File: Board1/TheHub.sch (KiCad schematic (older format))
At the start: 55 parts, among them J1 ARM_ADC_1, J10 SCIENCE + WHEELS POWER CONN, J11 RFD900, J12 I2C_1 Test Point, J13 I2C_2 Test Point, J14 ARDUINO NANO LEFT, J15 GPIO Test, J16 I2C_3 Test Point, J17 12V OUT, J18 7.4V IN, J19 ANALOG SENSORS, J2 ARM_ADC_2, J20 GPS, J21 COMPASS, J22 ARDUINO NANO RIGHT, J23 NucleoRight, J3 ARM_PWM_OUT, J4 ARM POWER CONN, J5 NucleoLeft, J6 SCI_ADC_1, J7 SCIENCE_PWM_OUT, J8 12V MAIN POWER, J9 WHEEL_ADC_1, U1 PRE-PCA9685, U2 PRE-ADS1115, U3 PRE-ADS1115, U4 PRE-PCA9685, U5 PRE-ADS1115, U6 TL1963, U7 LM340MP-5.0, U9 PRE-ADS1115

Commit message: Add note or BNO055, add GPS, add nucleo pin declaration for GPS_FIX GPIO_Input
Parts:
- added U?: ADXL377, symbol ADXL377
- added U?: BNO055, symbol BNO055
- added U?: MCP9808, symbol MCP9808
- added U?: MPL115A2, symbol MPL115A2
- added U?: GPS, symbol GPS
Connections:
- net labels added: GPS_FIX, PWM1, PWM2
- wire segments 150 -> 161
- no-connect marks 52 -> 70
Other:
- note added: "GPS_FIX is HIGH when\nthe unit has a GPS lock."
- note added: "PS0 and PS1 are protocol select pins. \nLeave them connected to ground through\n 10k resistors for standard/fast I2C.\n"
- moved on the sheet: D7, R13

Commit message: Annotate schematic
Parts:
- gave numbers to parts that had none: 5

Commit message: Add MPL115A2 footprint, annotate schematic
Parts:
- removed D7: LED, LEDs:LED_0805, symbol LED
- removed J1: ARM_ADC_1, Pin_Headers:Pin_Header_Straight_2x04_Pitch2.54mm, symbol CONN_02X04
- removed J10: SCIENCE + WHEELS POWER CONN, Pin_Headers:Pin_Header_Straight_2x19_Pitch2.54mm, symbol CONN_02X16
- removed J14: ARDUINO NANO LEFT, Socket_Strips:Socket_Strip_Straight_1x15_Pitch2.54mm, symbol CONN_01X15
- removed J19: ANALOG SENSORS, Pin_Headers:Pin_Header_Straight_2x05_Pitch2.54mm, symbol CONN_02X05
- removed J2: ARM_ADC_2, Pin_Headers:Pin_Header_Straight_2x04_Pitch2.54mm, symbol CONN_02X04
- removed J20: GPS, Socket_Strips:Socket_Strip_Straight_1x09_Pitch2.54mm, symbol CONN_01X09
- removed J21: COMPASS, Socket_Strips:Socket_Strip_Straight_1x06_Pitch2.54mm, symbol CONN_01X06
- removed J22: ARDUINO NANO RIGHT, Socket_Strips:Socket_Strip_Straight_1x15_Pitch2.54mm, symbol CONN_01X15
- removed J3: ARM_PWM_OUT, Pin_Headers:Pin_Header_Straight_1x16_Pitch2.54mm, symbol CONN_01X16
- removed J4: ARM POWER CONN, Pin_Headers:Pin_Header_Straight_2x16_Pitch2.54mm, symbol CONN_02X16
- removed J6: SCI_ADC_1, Pin_Headers:Pin_Header_Straight_2x04_Pitch2.54mm, symbol CONN_02X04
- removed J7: SCIENCE_PWM_OUT, Pin_Headers:Pin_Header_Straight_1x16_Pitch2.54mm, symbol CONN_01X16
- removed J9: WHEEL_ADC_1, Pin_Headers:Pin_Header_Straight_2x04_Pitch2.54mm, symbol CONN_02X04
- removed R13: 220, Resistors_SMD:R_0805, symbol R
- removed U1, U4: PRE-PCA9685, FoxWestern:PCA9685, symbol PRE-PCA9685
- removed U2, U3, U5, U9: PRE-ADS1115, Socket_Strips:Socket_Strip_Straight_1x10_Pitch2.54mm, symbol PRE-ADS1115
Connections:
- net labels removed: A3, A4, A5, A6, A7, D10, D11, D12, D13, D2, D3, D4, D5, D6, D7, D8, D9, REF, RX0, TX1, VIN
- wire segments 161 -> 88
- no-connect marks 70 -> 37
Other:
- note added: "1.0"
- note added: "1/8/2017"
- note added: "2.2k pullups allow for fast I2C. Test headers allow for easy testing."
- note added: "Lin reg for powering microcontroller + sensors"
- note added: "Lin regs used to save money and reduce noise and complexity"
- note added: "Made By: Danny Mallek"
- note added: "Test Board"
- note added: "lin reg for rfd900"
- note removed: "0X48\n"
- note removed: "0X49"
- note removed: "0X4A"
- note removed: "0X4B"
- note removed: "ARM CARD"
- note removed: "AUTONOMY CARD"
- note removed: "SCIENCE +WHEEL CARD"
- note removed: "SOLDER 00000: 0X40"
- note removed: "SOLDER 00001: 0X41"
- note removed: "USE ADAFRUIT HMC5883L\nFOR COMPATIBILITY"
- note removed: "USE ADAFRUIT ULTIMATE GPS\nFOR COMPATIBILITY"

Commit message: Associate parts using CvPCB
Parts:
- U10: footprint (none) -> FoxWestern:ADXL377
- U11: footprint (none) -> FoxWestern:BNO055
- U12: footprint (none) -> FoxWestern:MPL115A2
- U13: footprint (none) -> FoxWestern:Adafruit_GPS
- U8: footprint (none) -> FoxWestern:MCP9808
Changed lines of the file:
@@
 5V
 $Comp
-L +5V #PWR028
+L +5V #PWR014
 U 1 1 593718A3
 P 12650 1550
-F 0 "#PWR028" H 12650 1400 50  0001 C CNN
+F 0 "#PWR014" H 12650 1400 50  0001 C CNN
 F 1 "+5V" H 12650 1690 50  0000 C CNN
 F 2 "" H 12650 1550 50  0001 C CNN
@@
 $EndComp
 $Comp
-L GND #PWR029
+L GND #PWR015
 U 1 1 59371A35
 P 12150 1250
-F 0 "#PWR029" H 12150 1000 50  0001 C CNN
+F 0 "#PWR015" H 12150 1000 50  0001 C CNN
 F 1 "GND" H 12150 1100 50  0000 C CNN
 F 2 "" H 12150 1250 50  0001 C CNN
@@
 USART6_RX
 $Comp
-L GND #PWR030
+L GND #PWR016
 U 1 1 59372AF7
 P 12550 2150
-F 0 "#PWR030" H 12550 1900 50  0001 C CNN
+F 0 "#PWR016" H 12550 1900 50  0001 C CNN
 F 1 "GND" H 12550 2000 50  0000 C CNN
 F 2 "" H 12550 2150 50  0001 C CNN
@@
 $EndComp
 $Comp
-L GND #PWR031
+L GND #PWR017
 U 1 1 59376B06
 P 13250 2200
-F 0 "#PWR031" H 13250 1950 50  0001 C CNN
+F 0 "#PWR017" H 13250 1950 50  0001 C CNN
 F 1 "GND" H 13250 2050 50  0000 C CNN
 F 2 "" H 13250 2200 50  0001 C CNN
@@
 $EndComp
 $Comp
-L GND #PWR032
+L GND #PWR018
 U 1 1 593775C1
 P 14050 2200
-F 0 "#PWR032" H 14050 1950 50  0001 C CNN
+F 0 "#PWR018" H 14050 1950 50  0001 C CNN
 F 1 "GND" H 14050 2050 50  0000 C CNN
 F 2 "" H 14050 2200 50  0001 C CNN
@@
 $EndComp
 $Comp
-L GND #PWR033
+L GND #PWR019
 U 1 1 5937761C
 P 15050 2200
-F 0 "#PWR033" H 15050 1950 50  0001 C CNN
+F 0 "#PWR019" H 15050 1950 50  0001 C CNN
 F 1 "GND" H 15050 2050 50  0000 C CNN
 F 2 "" H 15050 2200 50  0001 C CNN
@@
 $EndComp
 $Comp
-L GND #PWR034
+L GND #PWR020
 U 1 1 5937D087
 P 13650 3350
-F 0 "#PWR034" H 13650 3100 50  0001 C CNN
+F 0 "#PWR020" H 13650 3100 50  0001 C CNN
 F 1 "GND" H 13650 3200 50  0000 C CNN
 F 2 "" H 13650 3350 50  0001 C CNN
@@
 $EndComp
 $Comp
-L +12V #PWR035
+L +12V #PWR021
 U 1 1 5937F443
 P 9250 3100
-F 0 "#PWR035" H 9250 2950 50  0001 C CNN
+F 0 "#PWR021" H 9250 2950 50  0001 C CNN
 F 1 "+12V" H 9250 3240 50  0000 C CNN
 F 2 "" H 9250 3100 50  0001 C CNN
@@
 $EndComp
 $Comp
-L +5V #PWR036
+L +5V #PWR022
 U 1 1 59380CDB
 P 10600 3050
-F 0 "#PWR036" H 10600 2900 50  0001 C CNN
+F 0 "#PWR022" H 10600 2900 50  0001 C CNN
 F 1 "+5V" H 10600 3190 50  0000 C CNN
 F 2 "" H 10600 3050 50  0001 C CNN
@@
 $EndComp
 $Comp
-L GND #PWR037
+L GND #PWR023
 U 1 1 59381160
 P 9900 3700
-F 0 "#PWR037" H 9900 3450 50  0001 C CNN
+F 0 "#PWR023" H 9900 3450 50  0001 C CNN
 F 1 "GND" H 9900 3550 50  0000 C CNN
 F 2 "" H 9900 3700 50  0001 C CNN
@@
 $EndComp
 $Comp
-L PWR_FLAG #FLG038
+L PWR_FLAG #FLG024
 U 1 1 59381518
 P 10600 1500
-F 0 "#FLG038" H 10600 1575 50  0001 C CNN
+F 0 "#FLG024" H 10600 1575 50  0001 C CNN
 F 1 "PWR_FLAG" H 10600 1650 50  0000 C CNN
 F 2 "" H 10600 1500 50  0001 C CNN
@@
 $EndComp
 $Comp
-L PWR_FLAG #FLG039
+L PWR_FLAG #FLG025
 U 1 1 59381757
 P 10600 3200
-F 0 "#FLG039" H 10600 3275 50  0001 C CNN
+F 0 "#FLG025" H 10600 3275 50  0001 C CNN
 F 1 "PWR_FLAG" H 10600 3350 50  0000 C CNN
 F 2 "" H 10600 3200 50  0001 C CNN
@@
 $EndComp
 $Comp
-L GND #PWR040
+L GND #PWR026
 U 1 1 59383C45
 P 11000 2250
-F 0 "#PWR040" H 11000 2000 50  0001 C CNN
+F 0 "#PWR026" H 11000 2000 50  0001 C CNN
 F 1 "GND" H 11000 2100 50  0000 C CNN
 F 2 "" H 11000 2250 50  0001 C CNN
@@
 $EndComp
 $Comp
-L GND #PWR041
+L GND #PWR027
 U 1 1 59383CE4
 P 11100 3700
-F 0 "#PWR041" H 11100 3450 50  0001 C CNN
+F 0 "#PWR027" H 11100 3450 50  0001 C CNN
 F 1 "GND" H 11100 3550 50  0000 C CNN
 F 2 "" H 11100 3700 50  0001 C CNN
@@
 $EndComp
 $Comp
-L +12V #PWR053
+L +12V #PWR028
 U 1 1 593A2E97
 P 7800 2100
-F 0 "#PWR053" H 7800 1950 50  0001 C CNN
+F 0 "#PWR028" H 7800 1950 50  0001 C CNN
 F 1 "+12V" H 7800 2240 50  0000 C CNN
 F 2 "" H 7800 2100 50  0001 C CNN
@@
 $EndComp
 $Comp
-L GND #PWR054
+L GND #PWR029
 U 1 1 593A2EA3
 P 7800 2300
-F 0 "#PWR054" H 7800 2050 50  0001 C CNN
+F 0 "#PWR029" H 7800 2050 50  0001 C CNN
 F 1 "GND" H 7800 2150 50  0000 C CNN
 F 2 "" H 7800 2300 50  0001 C CNN
@@
 $EndComp
 $Comp
-L GND #PWR055
+L GND #PWR030
 U 1 1 593A3BC4
 P 7800 3000
-F 0 "#PWR055" H 7800 2750 50  0001 C CNN
+F 0 "#PWR030" H 7800 2750 50  0001 C CNN
 F 1 "GND" H 7800 2850 50  0000 C CNN
 F 2 "" H 7800 3000 50  0001 C CNN
@@
 	3650 2650 4050 2650
 $Comp
-L +3V3 #PWR060
+L +3V3 #PWR031
 U 1 1 59365D75
 P 4050 2650
-F 0 "#PWR060" H 4050 2500 50  0001 C CNN
+F 0 "#PWR031" H 4050 2500 50  0001 C CNN
 F 1 "+3V3" H 4050 2790 50  0000 C CNN
 F 2 "" H 4050 2650 50  0001 C CNN
@@
 F 0 "U10" H 2950 4600 60  0000 C CNN
 F 1 "ADXL377" H 2800 5400 60  0000 C CNN
-F 2 "" H 2750 5150 60  0001 C CNN
+F 2 "FoxWestern:ADXL377" H 2750 5150 60  0001 C CNN
 F 3 "" H 2750 5150 60  0001 C CNN
 	1    2850 5150
@@
 F 0 "U11" H 5750 5400 60  0000 C CNN
 F 1 "BNO055" H 5550 6100 60  0000 C CNN
-F 2 "" H 5450 5500 60  0001 C CNN
+F 2 "FoxWestern:BNO055" H 5450 5500 60  0001 C CNN
 F 3 "" H 5450 5500 60  0001 C CNN
 	1    5450 5500
@@
 F 0 "U8" H 2950 5750 60  0000 C CNN
 F 1 "MCP9808" H 2800 6650 60  0000 C CNN
-F 2 "" H 2800 6350 60  0001 C CNN
+F 2 "FoxWestern:MCP9808" H 2800 6350 60  0001 C CNN
 F 3 "" H 2800 6350 60  0001 C CNN
 	1    2800 6350
@@
 F 0 "U12" H 5750 6400 60  0000 C CNN
 F 1 "MPL115A2" H 5550 7100 60  0000 C CNN
-F 2 "" H 5600 6600 60  0001 C CNN
+F 2 "FoxWestern:MPL115A2" H 5600 6600 60  0001 C CNN
 F 3 "" H 5600 6600 60  0001 C CNN
 	1    5550 6750
@@
 A2
 $Comp
-L GND #PWR061
+L GND #PWR032
 U 1 1 5A529AE0
 P 2350 5200
-F 0 "#PWR061" H 2350 4950 50  0001 C CNN
+F 0 "#PWR032" H 2350 4950 50  0001 C CNN
 F 1 "GND" H 2350 5050 50  0000 C CNN
 F 2 "" H 2350 5200 50  0001 C CNN
@@
 	2350 5200 2400 5200
 $Comp
-L +3V3 #PWR062
+L +3V3 #PWR033
 U 1 1 5A52A014
 P 2400 5000
-F 0 "#PWR062" H 2400 4850 50  0001 C CNN
+F 0 "#PWR033" H 2400 4850 50  0001 C CNN
 F 1 "+3V3" H 2400 5140 50  0000 C CNN
 F 2 "" H 2400 5000 50  0001 C CNN
@@
 NoConn ~ 2400 6550
 $Comp
-L +3V3 #PWR063
+L +3V3 #PWR034
 U 1 1 5A52B4C8
 P 2400 6150
-F 0 "#PWR063" H 2400 6000 50  0001 C CNN
+F 0 "#PWR034" H 2400 6000 50  0001 C CNN
 F 1 "+3V3" H 2400 6290 50  0000 C CNN
 F 2 "" H 2400 6150 50  0001 C CNN
@@
 $EndComp
 $Comp
-L GND #PWR064
+L GND #PWR035
 U 1 1 5A52B584
 P 2100 6250
-F 0 "#PWR064" H 2100 6000 50  0001 C CNN
+F 0 "#PWR035" H 2100 6000 50  0001 C CNN
 F 1 "GND" H 2100 6100 50  0000 C CNN
 F 2 "" H 2100 6250 50  0001 C CNN
@@
 SCL_1
 $Comp
-L +3V3 #PWR065
+L +3V3 #PWR036
 U 1 1 5A52EB6E
 P 5100 7000
-F 0 "#PWR065" H 5100 6850 50  0001 C CNN
+F 0 "#PWR036" H 5100 6850 50  0001 C CNN
 F 1 "+3V3" H 5100 7140 50  0000 C CNN
 F 2 "" H 5100 7000 50  0001 C CNN
@@
 $EndComp
 $Comp
-L GND #PWR066
+L GND #PWR037
 U 1 1 5A52EBF1
 P 4900 6900
-F 0 "#PWR066" H 4900 6650 50  0001 C CNN
+F 0 "#PWR037" H 4900 6650 50  0001 C CNN
 F 1 "GND" H 4900 6750 50  0000 C CNN
 F 2 "" H 4900 6900 50  0001 C CNN
@@
 NoConn ~ 5100 6500
 $Comp
-L +3V3 #PWR067
+L +3V3 #PWR038
 U 1 1 5A52F8E1
 P 5050 5000
-F 0 "#PWR067" H 5050 4850 50  0001 C CNN
+F 0 "#PWR038" H 5050 4850 50  0001 C CNN
 F 1 "+3V3" H 5050 5140 50  0000 C CNN
 F 2 "" H 5050 5000 50  0001 C CNN
@@
 $EndComp
 $Comp
-L GND #PWR068
+L GND #PWR039
 U 1 1 5A52F99D
 P 4800 5200
-F 0 "#PWR068" H 4800 4950 50  0001 C CNN
+F 0 "#PWR039" H 4800 4950 50  0001 C CNN
 F 1 "GND" H 4800 5050 50  0000 C CNN
 F 2 "" H 4800 5200 50  0001 C CNN
@@
 F 0 "U13" H 8400 6200 60  0000 C CNN
 F 1 "GPS" H 8200 7200 60  0000 C CNN
-F 2 "" H 8150 6950 60  0001 C CNN
+F 2 "FoxWestern:Adafruit_GPS" H 8150 6950 60  0001 C CNN
 F 3 "" H 8150 6950 60  0001 C CNN
 	1    8200 6700
@@
 $EndComp
 $Comp
-L +3V3 #PWR069
+L +3V3 #PWR040
 U 1 1 5A533C10
 P 7750 7000
-F 0 "#PWR069" H 7750 6850 50  0001 C CNN
+F 0 "#PWR040" H 7750 6850 50  0001 C CNN
 F 1 "+3V3" H 7750 7140 50  0000 C CNN
 F 2 "" H 7750 7000 50  0001 C CNN
@@
 $EndComp
 $Comp
-L GND #PWR070
+L GND #PWR041
 U 1 1 5A533CCF
 P 7550 6900
-F 0 "#PWR070" H 7550 6650 50  0001 C CNN
+F 0 "#PWR041" H 7550 6650 50  0001 C CNN
 F 1 "GND" H 7550 6750 50  0000 C CNN
 F 2 "" H 7550 6900 50  0001 C CNN

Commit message: Add to schematic and CubeMX: IO for SD card datalogger, 2x analog pot inputs, quad encoder
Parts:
- added J?: Actuator Fdbk Conn, symbol Conn_02x03_Odd_Even
- added J?: QuadEnc_Conn, symbol Conn_01x04
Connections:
- net +3V3: now also J?.1 (Pin_1), J?.3 (Pin_3), J?.4 (Pin_4)
- net GND: now also J?.4 (Pin_4), J?.5 (Pin_5), J?.6 (Pin_6)
- net PB13: now also J?.3 (Pin_3)
- net PB14: now also J?.2 (Pin_2)
- net PC0 renamed A_FDBK_1
- net A_FDBK_1: now also J?.2 (Pin_2)
- net PC1 renamed A_FDBK_0
- net A_FDBK_0: now also J?.1 (Pin_1)
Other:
- note added: "With 220Ohm, each led pulls 5mA, for a total of 20mA.\nDo not exceed 200mA for entire chip and 20mA per pin group."
- note removed: "With 220Ohm, each led pulls 5mA, for a total of 20mA."
- moved on the sheet: J5

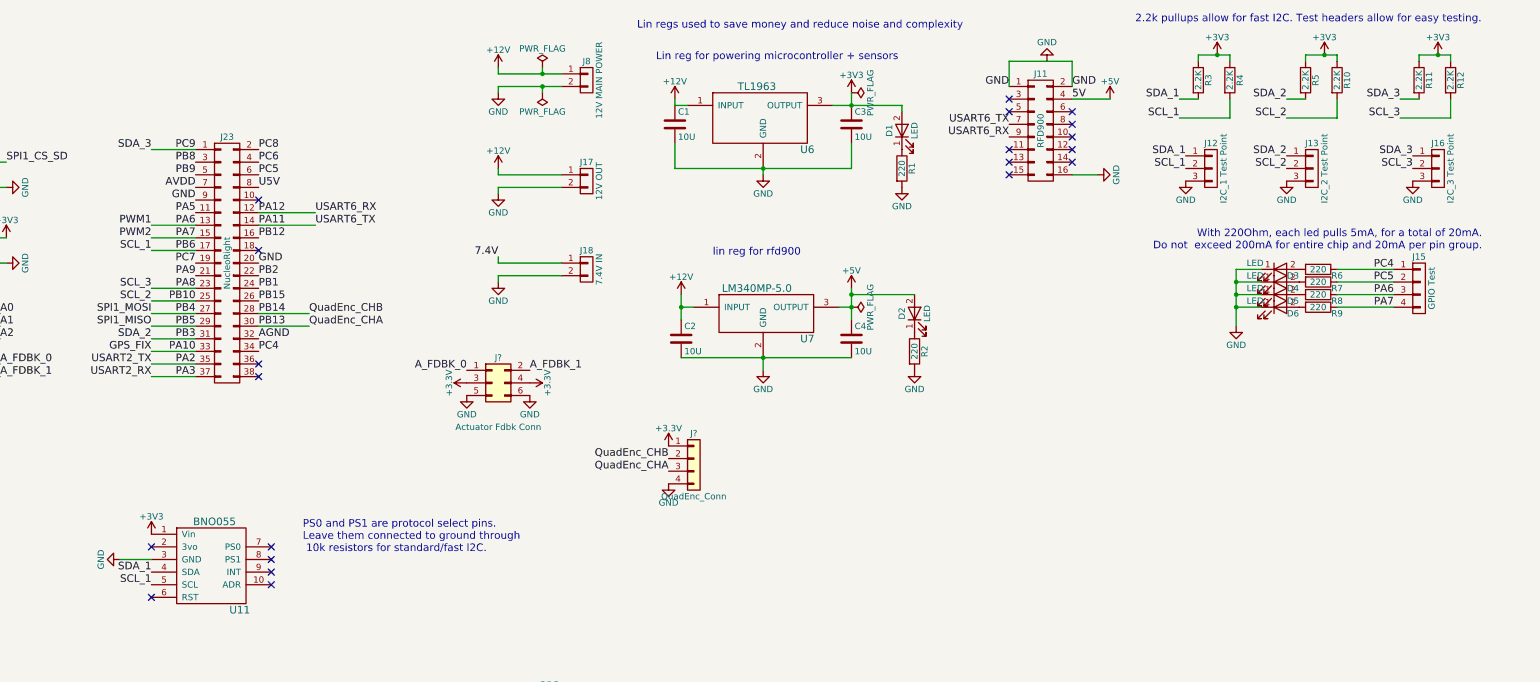
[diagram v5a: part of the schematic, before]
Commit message: Add Datalogger library schematic and integrate into schematic
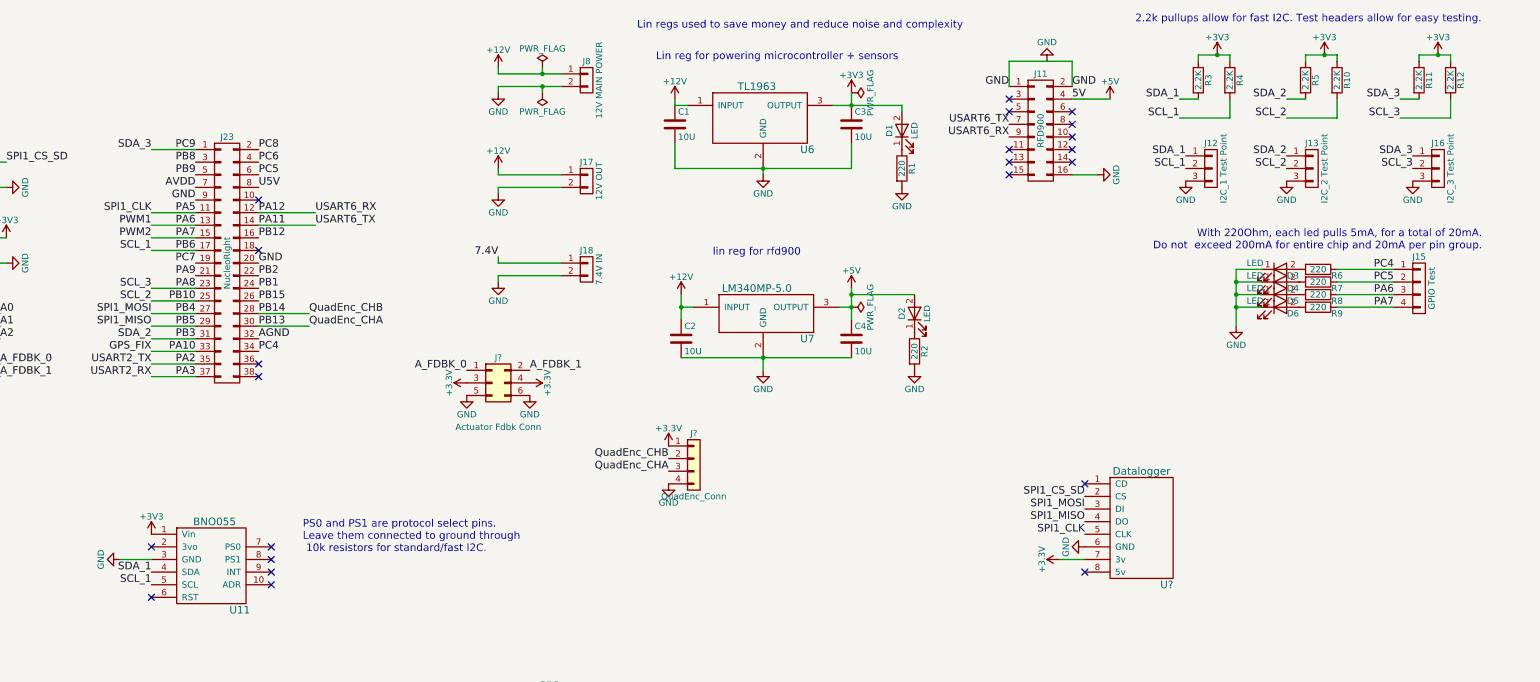
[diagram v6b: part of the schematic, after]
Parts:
- added U?: Datalogger, symbol Datalogger
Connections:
- net +3V3: now also U?.7 (3v)
- net GND: now also U?.6 (GND)
- net PA5: now also U?.5 (CLK)
- net PB4: now also U?.3 (DI)
- net PB5: now also U?.4 (DO)
- net PD2: now also U?.2 (CS)
- no-connect marks 37 -> 39
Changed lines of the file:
@@
 	10600 1500 10600 1600
 Wire Wire Line
-	10450 1600 10600 1600
-Wire Wire Line
-	10600 1600 11000 1600
+	10450 1600 11000 1600
 Wire Wire Line
 	7800 1300 7800 1350
 Wire Wire Line
-	7800 1350 8150 1350
-Wire Wire Line
-	8150 1350 8300 1350
+	7800 1350 8300 1350
 Wire Wire Line
 	8150 1300 8150 1350
@@
 	7800 1500 7800 1450
 Wire Wire Line
-	7800 1450 8150 1450
-Wire Wire Line
-	8150 1450 8300 1450
+	7800 1450 8300 1450
 Wire Wire Line
 	8150 1500 8150 1450
@@
 	15100 1250 15100 1200
 Wire Wire Line
-	15100 1200 15250 1200
-Wire Wire Line
-	15250 1200 15350 1200
+	15100 1200 15350 1200
 Wire Wire Line
 	14950 1700 15350 1700
@@
 	13350 1250 13350 1200
 Wire Wire Line
-	13350 1200 13500 1200
-Wire Wire Line
-	13500 1200 13600 1200
+	13350 1200 13600 1200
 Wire Wire Line
 	13200 1700 13600 1700
@@
 	14200 1250 14200 1200
 Wire Wire Line
-	14200 1200 14350 1200
-Wire Wire Line
-	14350 1200 14450 1200
+	14200 1200 14450 1200
 Wire Wire Line
 	14050 1700 14450 1700
@@
 	9200 1900 9200 2100
 Wire Wire Line
-	9200 2100 9900 2100
-Wire Wire Line
-	9900 2100 10600 2100
+	9200 2100 10600 2100
 Wire Wire Line
 	10600 2100 10600 1900
@@
 	14450 3200 14900 3200
 Wire Wire Line
-	13650 2900 13650 3000
-Wire Wire Line
-	13650 3000 13650 3100
-Wire Wire Line
-	13650 3100 13650 3200
-Wire Wire Line
-	13650 3200 13650 3350
+	13650 2900 13650 3350
 Wire Wire Line
 	13650 2900 13850 2900
@@
 Connection ~ 13650 3200
 Wire Wire Line
-	9250 3100 9250 3200
-Wire Wire Line
-	9250 3200 9250 3300
+	9250 3100 9250 3300
 Wire Wire Line
 	9250 3200 9350 3200
 Connection ~ 9250 3200
 Wire Wire Line
-	10600 3050 10600 3100
-Wire Wire Line
-	10600 3100 10600 3200
-Wire Wire Line
-	10600 3200 10600 3300
+	10600 3050 10600 3300
 Wire Wire Line
 	10500 3200 10600 3200
 Connection ~ 10600 3200
 Wire Wire Line
-	9250 3600 9900 3600
-Wire Wire Line
-	9900 3600 10600 3600
+	9250 3600 10600 3600
 Connection ~ 9900 3600
 Wire Wire Line
@@
 	1    0    0    -1
 $EndComp
+$Comp
+L Datalogger U?
+U 1 1 5A670F4A
+P 12650 5500
+F 0 "U?" H 13100 5600 60  0000 C CNN
+F 1 "Datalogger" H 12900 6500 60  0000 C CNN
+F 2 "" H 12650 5500 60  0001 C CNN
+F 3 "" H 12650 5500 60  0001 C CNN
+	1    12650 5500
+	1    0    0    -1
+$EndComp
+Text Label 12450 4700 2    60   ~ 0
+SPI1_CS_SD
+Text Label 12450 4800 2    60   ~ 0
+SPI1_MOSI
+Text Label 12450 4900 2    60   ~ 0
+SPI1_MISO
+Wire Wire Line
+	5400 2450 5050 2450
+Text Label 5050 2450 2    60   ~ 0
+SPI1_CLK
+Text Label 12450 5000 2    60   ~ 0
+SPI1_CLK
+$Comp
+L GND #PWR?
+U 1 1 5A676B6D
+P 12450 5100
+F 0 "#PWR?" H 12450 4850 50  0001 C CNN
+F 1 "GND" H 12450 4950 50  0000 C CNN
+F 2 "" H 12450 5100 50  0001 C CNN
+F 3 "" H 12450 5100 50  0001 C CNN
+	1    12450 5100
+	0    1    1    0
+$EndComp
+$Comp
+L +3.3V #PWR?
+U 1 1 5A676BD5
+P 12250 5200
+F 0 "#PWR?" H 12250 5050 50  0001 C CNN
+F 1 "+3.3V" H 12250 5340 50  0000 C CNN
+F 2 "" H 12250 5200 50  0001 C CNN
+F 3 "" H 12250 5200 50  0001 C CNN
+	1    12250 5200
+	0    -1   -1   0
+$EndComp
+Wire Wire Line
+	12250 5200 12450 5200
+NoConn ~ 12450 4600
+NoConn ~ 12450 5300
 $EndSCHEMATC
